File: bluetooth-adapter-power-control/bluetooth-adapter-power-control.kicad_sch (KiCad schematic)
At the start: 14 parts, among them J1 UPDI, J2 Conn_01x07_Socket, Q1 NMOS, U1 ATtiny202-SSNR

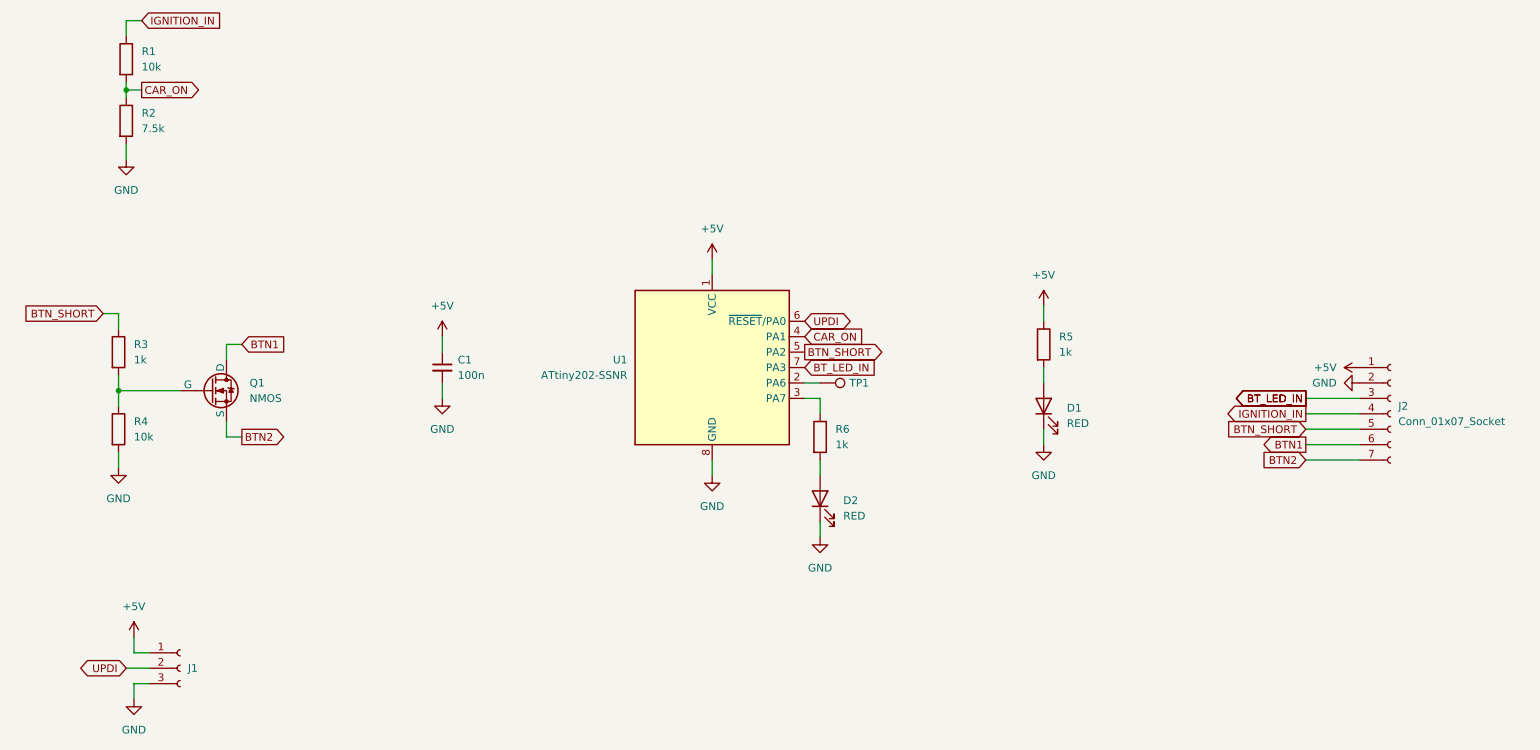
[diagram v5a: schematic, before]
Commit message: bluetooth-adapter-power-control: Switch UPDI header to have GND in the middle
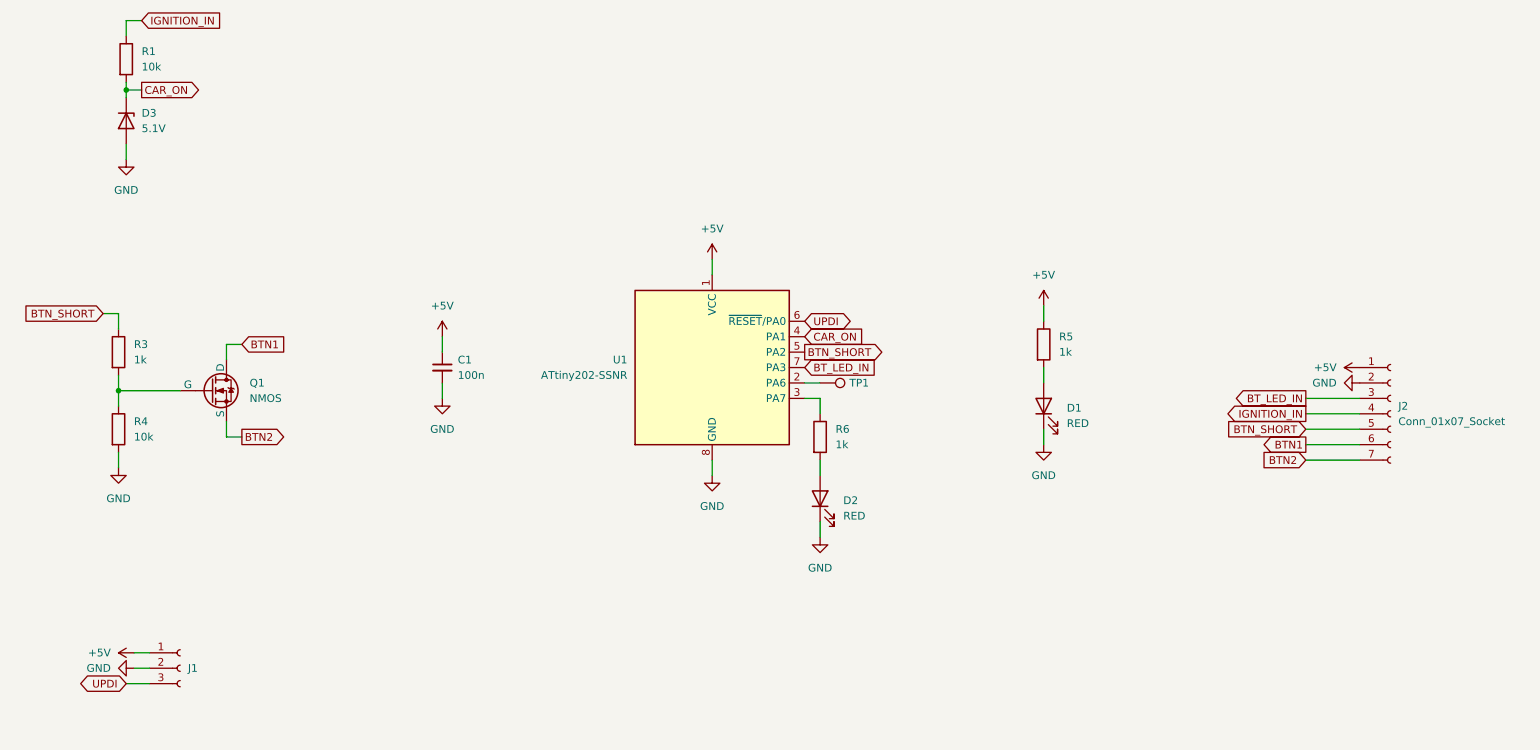
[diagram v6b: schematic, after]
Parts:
- removed R2: 7.5k, Resistor_SMD:R_0603_1608Metric, symbol Device:R
- added D3: 5.1V, Diode_SMD:D_SOD-523, symbol Device:D_Zener
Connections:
- net CAR_ON: now also D3.1 (K)
- net GND: now also J1.2 (Pin_2), D3.2 (A); no longer J1.3 (Pin_3)
- net UPDI: now also J1.3 (Pin_3); no longer J1.2 (Pin_2)
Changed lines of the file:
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@@
 	(wire
 		(pts
-			(xy 43.18 147.32) (xy 43.18 144.78)
+			(xy 43.18 149.86) (xy 45.72 149.86)
 		)
 		(stroke
@@
 	(wire
 		(pts
-			(xy 43.18 152.4) (xy 43.18 154.94)
-		)
-		(stroke
-			(width 0)
-			(type default)
-		)
-	)
-	(wire
-		(pts
-			(xy 45.72 152.4) (xy 43.18 152.4)
-		)
-		(stroke
-			(width 0)
-			(type default)
-		)
-	)
-	(wire
-		(pts
 			(xy 40.64 114.3) (xy 40.64 116.84)
 		)
@@
 	(wire
 		(pts
+			(xy 41.91 152.4) (xy 45.72 152.4)
+		)
+		(stroke
+			(width 0)
+			(type default)
+		)
+	)
+	(wire
+		(pts
 			(xy 156.21 125.73) (xy 156.21 128.27)
 		)
@@
 		(pts
 			(xy 193.04 110.49) (xy 193.04 113.03)
-		)
-		(stroke
-			(width 0)
-			(type default)
-		)
-	)
-	(wire
-		(pts
-			(xy 41.91 149.86) (xy 45.72 149.86)
 		)
 		(stroke
@@
 	(global_label "UPDI"
 		(shape bidirectional)
-		(at 41.91 149.86 180)
+		(at 41.91 152.4 180)
 		(fields_autoplaced yes)
 		(effects
@@
 		)
 		(property "Intersheetrefs" "${INTERSHEET_REFS}"
-			(at 33.3382 149.86 0)
+			(at 33.3382 152.4 0)
 			(effects
 				(font
@@
 		(property "Intersheetrefs" "${INTERSHEET_REFS}"
 			(at 222.591 110.49 0)
-			(effects
-				(font
-					(size 1.27 1.27)
-				)
-				(justify right)
-				(hide yes)
-			)
-		)
-	)
-	(global_label "BT_LED_IN"
-		(shape output)
-		(at 236.22 105.41 180)
-		(fields_autoplaced yes)
-		(effects
-			(font
-				(size 1.27 1.27)
-			)
-			(justify right)
-		)
-		(property "Intersheetrefs" "${INTERSHEET_REFS}"
-			(at 223.6796 105.41 0)
 			(effects
 				(font
@@
 	(symbol
 		(lib_id "power:+5V")
-		(at 43.18 144.78 0)
+		(at 43.18 147.32 90)
 		(unit 1)
 		(exclude_from_sim no)
@@
 		(fields_autoplaced yes)
 		(property "Reference" "#PWR05"
-			(at 43.18 148.59 0)
+			(at 46.99 147.32 0)
 			(effects
 				(font
@@
 		)
 		(property "Value" "+5V"
-			(at 43.18 139.7 0)
-			(effects
-				(font
-					(size 1.27 1.27)
-				)
+			(at 39.37 147.3199 90)
+			(effects
+				(font
+					(size 1.27 1.27)
+				)
+				(justify left)
 			)
 		)
 		(property "Footprint" ""
-			(at 43.18 144.78 0)
+			(at 43.18 147.32 0)
 			(effects
 				(font
@@
 		)
 		(property "Datasheet" ""
-			(at 43.18 144.78 0)
+			(at 43.18 147.32 0)
 			(effects
 				(font
@@
 		)
 		(property "Description" "Power symbol creates a global label with name \"+5V\""
-			(at 43.18 144.78 0)
+			(at 43.18 147.32 0)
 			(effects
 				(font
@@
 	)
 	(symbol
+		(lib_id "Device:D_Zener")
+		(at 41.91 59.69 270)
+		(unit 1)
+		(exclude_from_sim no)
+		(in_bom yes)
+		(on_board yes)
+		(dnp no)
+		(fields_autoplaced yes)
+		(property "Reference" "D3"
+			(at 44.45 58.4199 90)
+			(effects
+				(font
+					(size 1.27 1.27)
+				)
+				(justify left)
+			)
+		)
+		(property "Value" "5.1V"
+			(at 44.45 60.9599 90)
+			(effects
+				(font
+					(size 1.27 1.27)
+				)
+				(justify left)
+			)
+		)
+		(property "Footprint" "Diode_SMD:D_SOD-523"
+			(at 41.91 59.69 0)
+			(effects
+				(font
+					(size 1.27 1.27)
+				)
+				(hide yes)
+			)
+		)
+		(property "Datasheet" "~"
+			(at 41.91 59.69 0)
+			(effects
+				(font
+					(size 1.27 1.27)
+				)
+				(hide yes)
+			)
+		)
+		(property "Description" "Zener diode"
+			(at 41.91 59.69 0)
+			(effects
+				(font
+					(size 1.27 1.27)
+				)
+				(hide yes)
+			)
+		)
+		(pin "1"
+		)
+		(pin "2"
+		)
+		(instances
+			(project ""
+				(path "/cb952256-1cf9-427a-8657-67ac3ee7eb3e"
+					(reference "D3")
+					(unit 1)
+				)
+			)
+		)
+	)
+	(symbol
 		(lib_id "Connector:TestPoint")
 		(at 156.21 102.87 270)
@@
 	(symbol
 		(lib_id "Device:R")
-		(at 41.91 59.69 0)
-		(unit 1)
-		(exclude_from_sim no)
-		(in_bom yes)
-		(on_board yes)
-		(dnp no)
-		(fields_autoplaced yes)
-		(property "Reference" "R2"
-			(at 44.45 58.4199 0)
-			(effects
-				(font
-					(size 1.27 1.27)
-				)
-				(justify left)
-			)
-		)
-		(property "Value" "7.5k"
-			(at 44.45 60.9599 0)
-			(effects
-				(font
-					(size 1.27 1.27)
-				)
-				(justify left)
-			)
-		)
-		(property "Footprint" "Resistor_SMD:R_0603_1608Metric"
-			(at 40.132 59.69 90)
-			(effects
-				(font
-					(size 1.27 1.27)
-				)
-				(hide yes)
-			)
-		)
-		(property "Datasheet" "~"
-			(at 41.91 59.69 0)
-			(effects
-				(font
-					(size 1.27 1.27)
-				)
-				(hide yes)
-			)
-		)
-		(property "Description" "Resistor"
-			(at 41.91 59.69 0)
-			(effects
-				(font
-					(size 1.27 1.27)
-				)
-				(hide yes)
-			)
-		)
-		(pin "1"
-		)
-		(pin "2"
-		)
-		(instances
-			(project "bluetooth-adapter-power-control"
-				(path "/cb952256-1cf9-427a-8657-67ac3ee7eb3e"
-					(reference "R2")
-					(unit 1)
-				)
-			)
-		)
-	)
-	(symbol
-		(lib_id "Device:R")
 		(at 193.04 96.52 0)
 		(unit 1)
@@
 	(symbol
 		(lib_id "power:GND")
-		(at 43.18 154.94 0)
+		(at 43.18 149.86 270)
 		(unit 1)
 		(exclude_from_sim no)
@@
 		(fields_autoplaced yes)
 		(property "Reference" "#PWR06"
-			(at 43.18 161.29 0)
+			(at 36.83 149.86 0)
 			(effects
 				(font
@@
 		)
 		(property "Value" "GND"
-			(at 43.18 160.02 0)
-			(effects
-				(font
-					(size 1.27 1.27)
-				)
+			(at 39.37 149.8599 90)
+			(effects
+				(font
+					(size 1.27 1.27)
+				)
+				(justify right)
 			)
 		)
 		(property "Footprint" ""
-			(at 43.18 154.94 0)
+			(at 43.18 149.86 0)
 			(effects
 				(font
@@
 		)
 		(property "Datasheet" ""
-			(at 43.18 154.94 0)
+			(at 43.18 149.86 0)
 			(effects
 				(font
@@
 		)
 		(property "Description" "Power symbol creates a global label with name \"GND\" , ground"
-			(at 43.18 154.94 0)
-			(effects
-				(font
+			(at 43.18 149.86 0)
+			(effects
+				(font
